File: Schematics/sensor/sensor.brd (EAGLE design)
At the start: 23.8 x 16.5 mm, 16 parts, among them Y1 16MHz

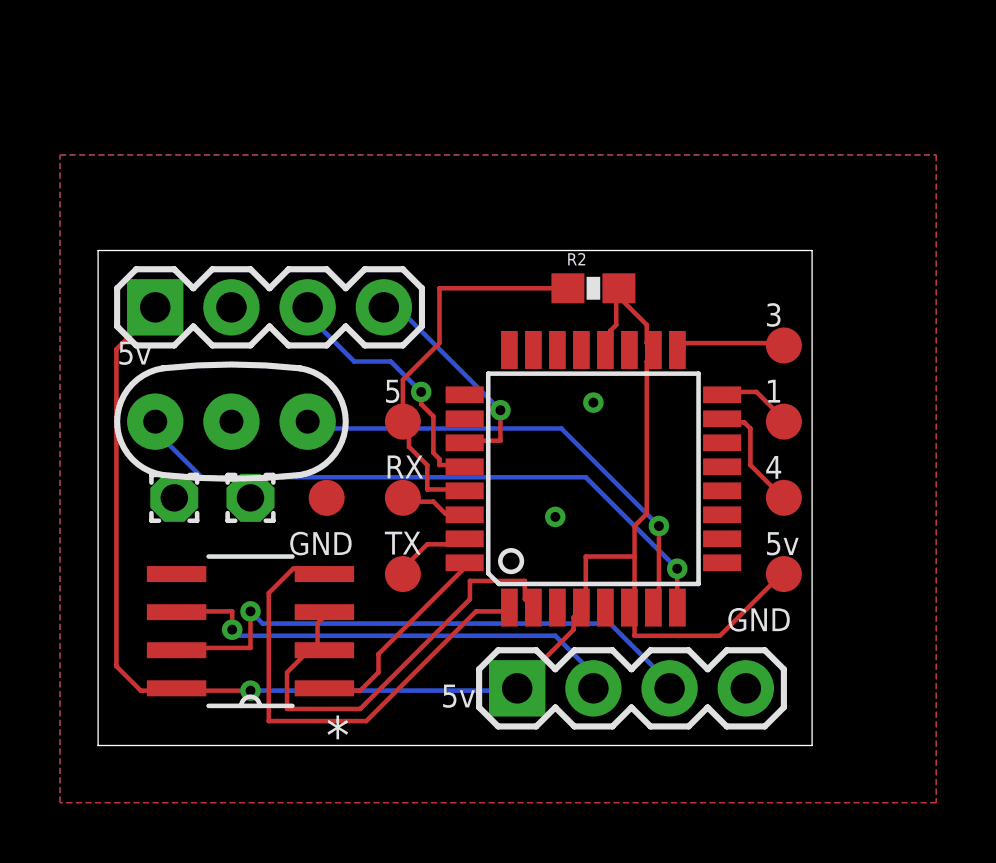
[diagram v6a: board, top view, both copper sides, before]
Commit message: PCB improvements
Node_SP 2.0: moved some text to the back layer

Sen_SP 4.0: improved the board for programming and changed the
resonator from through hole to surface mount - then rearranged the
items on the board to make it smaller
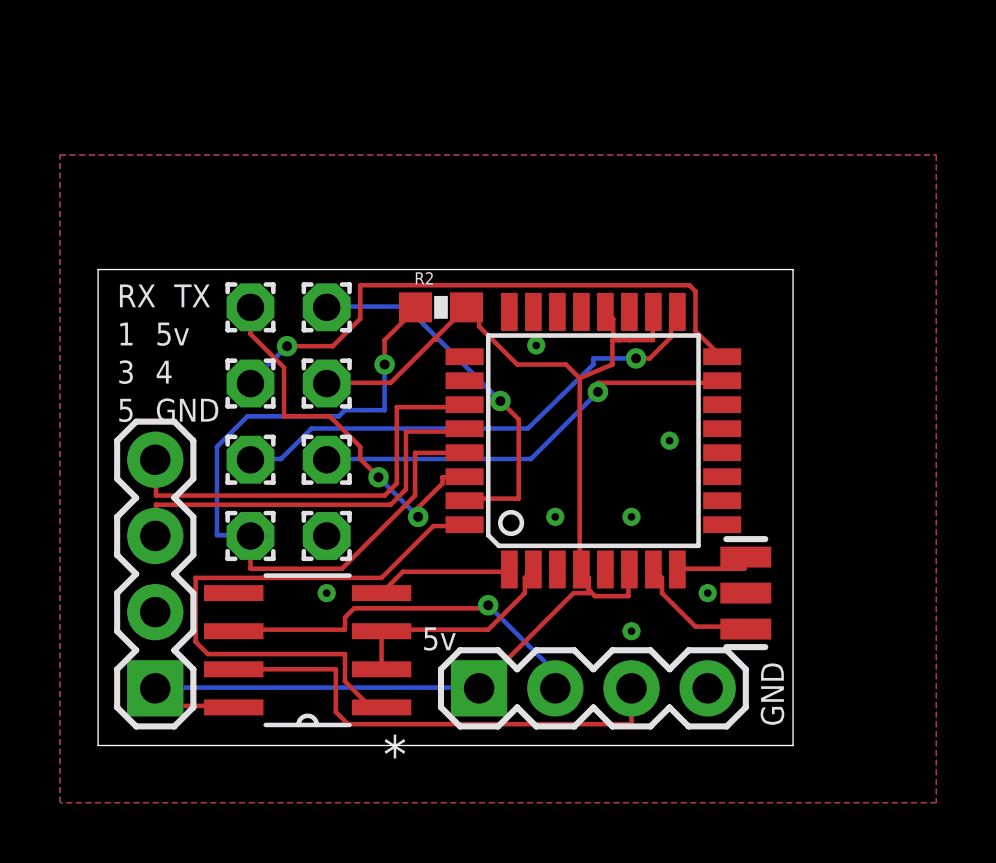
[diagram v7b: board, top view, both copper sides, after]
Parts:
- removed 15P, 16P, 17P, 5VP, GP, RST, RX, TX: PTR1TP12R, testpad:TP12R
- removed Y1: 16MHz, SparkFun-FreqCtrl:RESONATOR-PTH
- added PAD3, PAD4, PAD5, PAD6, PAD7, PAD8: (no value), wirepad:1,6/0,9
- added Y2: 16MHz, SparkFun-FreqCtrl:RESONATOR-SMD
- moved JP2 12.7 mm to (1.91, 1.91), turned to 90 degrees
- moved PAD2 8.13 mm to (7.62, 14.6)
- moved R2 5.12 mm to (11.4, 14.6)
- moved PAD1 2.84 mm to (7.62, 6.99)
- moved MAX485 2.01 mm to (6.99, 3.17)
- moved JP1 1.27 mm to (12.7, 1.91)
- moved ATMEGA328P 1.27 mm to (16.5, 10.2)
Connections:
- removed net N$3: 17P.TP, ATMEGA328P.17
- removed net N$4: 16P.TP, ATMEGA328P.16
- removed net N$5: 15P.TP, ATMEGA328P.15
- new net 1: ATMEGA328P.16, PAD5.1
- new net 3: ATMEGA328P.17, PAD4.1
- new net 4: ATMEGA328P.15, PAD6.1
- net 5V: now also PAD7.1; no longer 5VP.TP
- net GND: now also PAD1.1, Y2.2; no longer GP.TP, Y1.2
- net N$1: now also Y2.1; no longer Y1.1
- net N$2: now also Y2.3; no longer Y1.3
- net N$6: now also PAD3.1; no longer RX.TP
- net N$9: now also PAD2.1; no longer TX.TP
- net RESET: now also PAD8.1; no longer RST.TP
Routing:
- net 1: track 0.00 -> 19.5 mm, vias 0 -> 1
- net N$2: track 21.0 -> 2.63 mm, vias 1 -> 0
- net 3: track 0.00 -> 16.8 mm, vias 0 -> 1
- net 4: track 0.00 -> 14.5 mm, vias 0 -> 1
- net RO: track 6.90 -> 19.5 mm
- net N$1: track 16.0 -> 4.21 mm, vias 1 -> 0
- net DI: track 16.2 -> 4.58 mm
- net RESET: track 13.1 -> 24.7 mm, vias 0 -> 1
- net N$6: track 2.37 -> 12.6 mm, vias 0 -> 2
- net N$9: track 2.73 -> 12.5 mm, vias 0 -> 1
- net 5V: track 54.0 -> 45.6 mm, vias 1 -> 0
- net RW: track 15.6 -> 7.51 mm
- net SDA: track 7.61 -> 14.3 mm, vias 1 -> 0
- net SCL: track 8.71 -> 13.6 mm, vias 1 -> 0
- net N$5: track 3.86 -> 0.00 mm
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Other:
- board size 23.8 x 16.5 mm -> 23.2 x 15.9 mm
- board text added: "RX"
- board text added: "Sen_SP 4.0"
- board text added: "TX"
- board text removed: "SPSen 3.0"
